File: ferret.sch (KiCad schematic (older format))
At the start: 75 parts, among them J1 USB_C_Receptacle, J2 Jack-DC, J3 GND/RS485 L, J4 BAT+ L, J5 GND/RS485 R, J6 BAT+ R, J7 BAT, J8 Jack-DC, J9 SYS, Q1 40V, Q2 40V, Q3 40V, Q4 40V, Q5 40V, U1 FUSB307BMPX, U2 TPD6S300A, U3 BQ25792, U4 TPS560430X3F

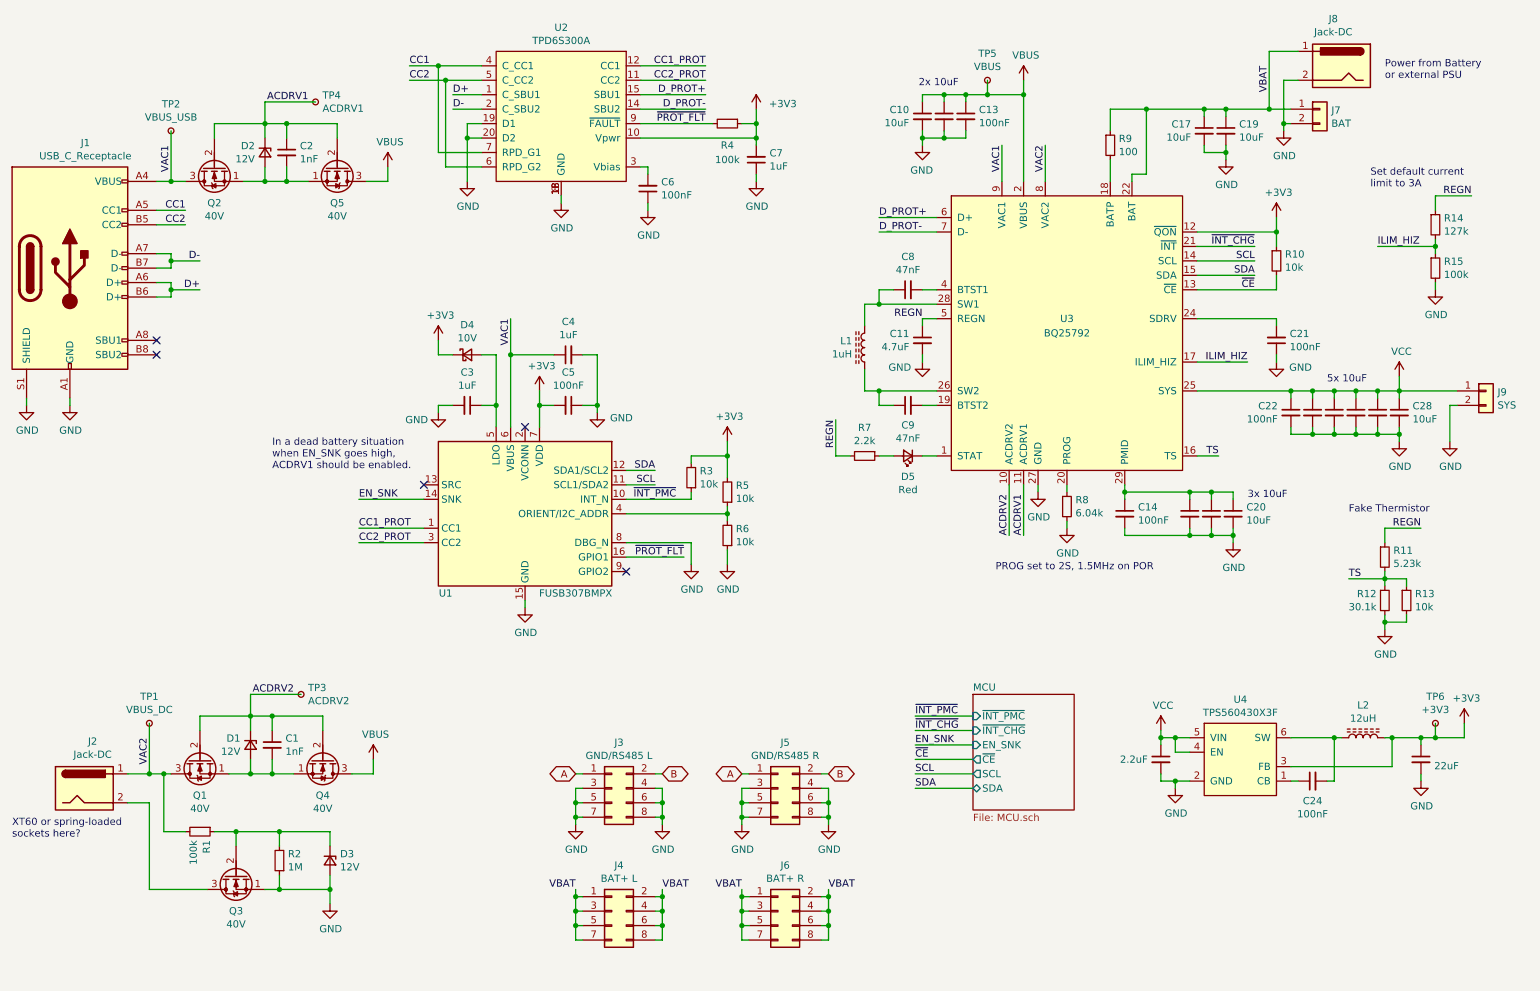
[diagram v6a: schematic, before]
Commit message: Split up ferret sheets and add some features
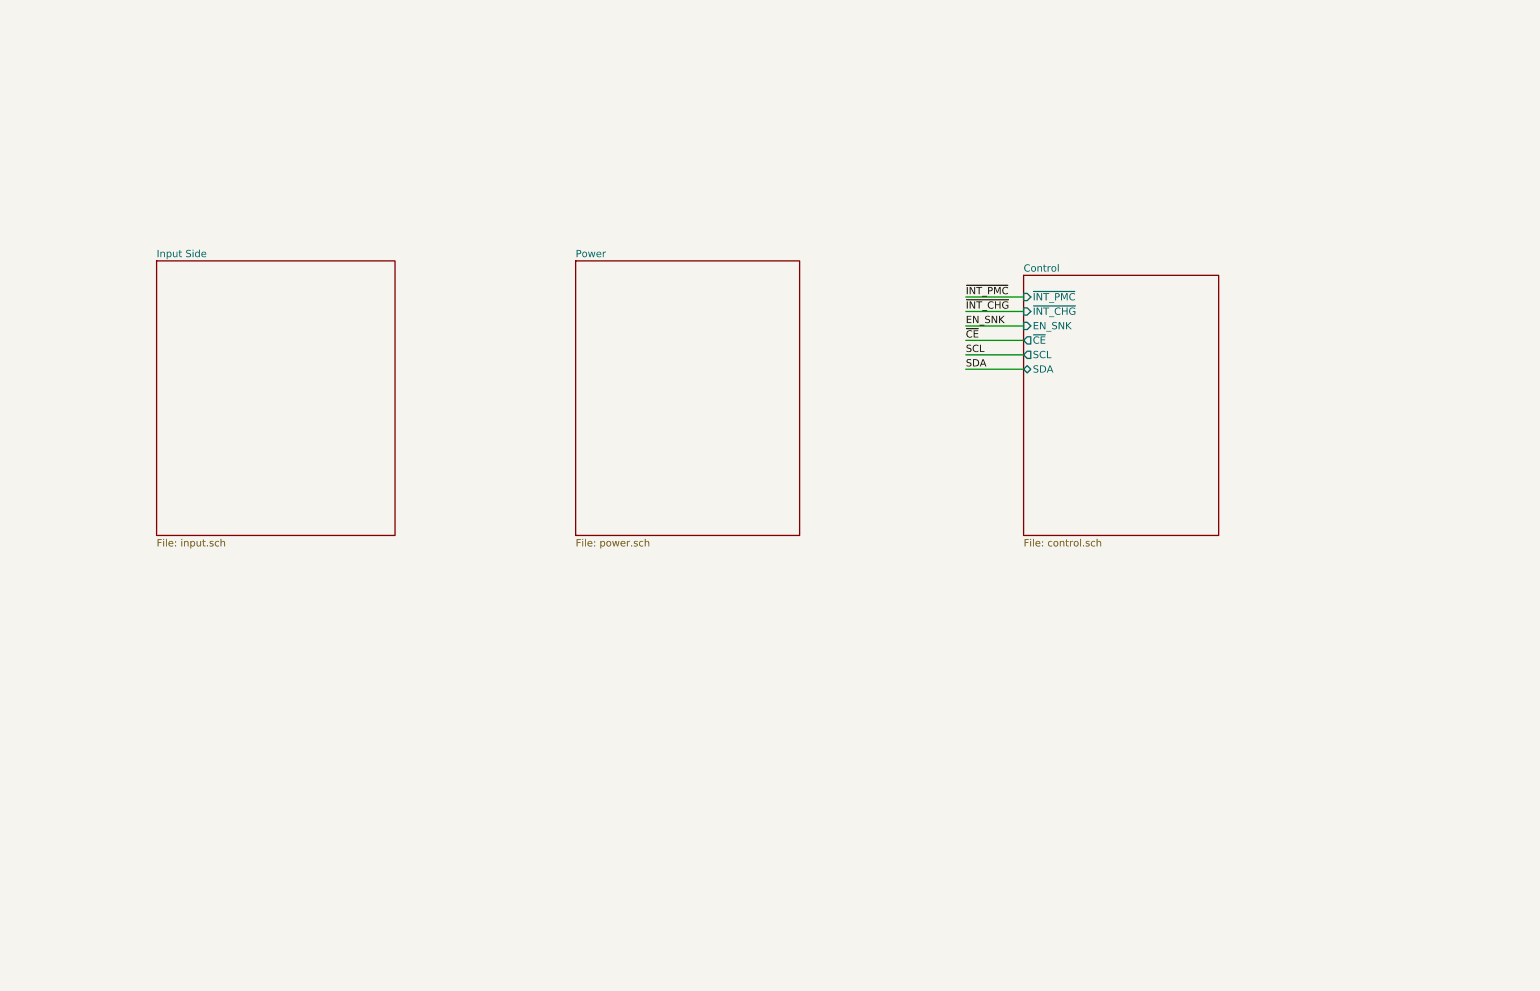
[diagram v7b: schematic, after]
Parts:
- removed C1, C2: 1nF, Capacitor_SMD:C_0603_1608Metric, symbol Device:C_Small
- removed C10, C12, C16, C17, C18, C19, C20, C23, C25, C26, C27, C28: 10uF, Capacitor_SMD:C_0805_2012Metric, symbol Device:C_Small
- removed C11: 4.7uF, Capacitor_SMD:C_0603_1608Metric, symbol Device:C_Small
- removed C13, C14, C21, C22, C24, C5, C6: 100nF, Capacitor_SMD:C_0603_1608Metric, symbol Device:C_Small
- removed C15: 2.2uF, Capacitor_SMD:C_0805_2012Metric, symbol Device:C_Small
- removed C29: 22uF, Capacitor_SMD:C_0805_2012Metric, symbol Device:C_Small
- removed C3, C4, C7: 1uF, Capacitor_SMD:C_0603_1608Metric, symbol Device:C_Small
- removed C8, C9: 47nF, Capacitor_SMD:C_0603_1608Metric, symbol Device:C_Small
- removed D1, D2, D3: 12V, Diode_SMD:D_SOD-523, symbol Device:D_Zener_Small
- removed D4: 10V, Diode_SMD:D_SOD-123, symbol Device:D_Schottky_Small
- removed D5: Red, LED_SMD:LED_0603_1608Metric_Castellated, symbol Device:LED_Small
- removed J1: USB_C_Receptacle, Connector_USB:USB_C_Receptacle_XKB_U262-16XN-4BVC11, symbol Connector:USB_C_Receptacle_USB2.0
- removed J2, J8: Jack-DC, Connector_BarrelJack:BarrelJack_Horizontal, symbol Connector:Jack-DC
- removed J3: GND/RS485 L, Connector_PinHeader_2.54mm:PinHeader_2x04_P2.54mm_Horizontal, symbol Connector_Generic:Conn_02x04_Odd_Even
- removed J4: BAT+ L, Connector_PinHeader_2.54mm:PinHeader_2x04_P2.54mm_Horizontal, symbol Connector_Generic:Conn_02x04_Odd_Even
- removed J5: GND/RS485 R, Connector_PinHeader_2.54mm:PinHeader_2x04_P2.54mm_Horizontal, symbol Connector_Generic:Conn_02x04_Odd_Even
- removed J6: BAT+ R, Connector_PinHeader_2.54mm:PinHeader_2x04_P2.54mm_Horizontal, symbol Connector_Generic:Conn_02x04_Odd_Even
- removed J7: BAT, Automated:Conn_AMASS_XT60PW-F20, symbol Connector_Generic:Conn_01x02
- removed J9: SYS, Connector_PinSocket_2.54mm:PinSocket_1x02_P2.54mm_Vertical, symbol Connector_Generic:Conn_01x02
- removed L1: 1uH, Inductor_SMD:L_Bourns_SRP1245A, symbol Device:L_Core_Ferrite
- removed L2: 12uH, Inductor_SMD:L_Bourns_SRN6045TA, symbol Device:L_Core_Ferrite
- removed Q1, Q2, Q3, Q4, Q5: 40V, Package_SO:Vishay_PowerPAK_1212-8_Single, symbol Device:Q_NMOS_SGD
- removed R1, R15, R4: 100k, Resistor_SMD:R_0603_1608Metric, symbol Device:R_Small
- removed R10, R13, R3, R5, R6: 10k, Resistor_SMD:R_0603_1608Metric, symbol Device:R_Small
- removed R11: 5.23k, Resistor_SMD:R_0603_1608Metric, symbol Device:R_Small
- removed R12: 30.1k, Resistor_SMD:R_0603_1608Metric, symbol Device:R_Small
- removed R14: 127k, Resistor_SMD:R_0603_1608Metric, symbol Device:R_Small
- removed R2: 1M, Resistor_SMD:R_0603_1608Metric, symbol Device:R_Small
- removed R7: 2.2k, Resistor_SMD:R_0603_1608Metric, symbol Device:R_Small
- removed R8: 6.04k, Resistor_SMD:R_0603_1608Metric, symbol Device:R_Small
- removed R9: 100, Resistor_SMD:R_0603_1608Metric, symbol Device:R_Small
- removed TP1: VBUS_DC, TestPoint:TestPoint_THTPad_D2.0mm_Drill1.0mm, symbol Connector:TestPoint_Small
- removed TP2: VBUS_USB, TestPoint:TestPoint_THTPad_D2.0mm_Drill1.0mm, symbol Connector:TestPoint_Small
- removed TP3: ACDRV2, TestPoint:TestPoint_THTPad_D2.0mm_Drill1.0mm, symbol Connector:TestPoint_Small
- removed TP4: ACDRV1, TestPoint:TestPoint_THTPad_D2.0mm_Drill1.0mm, symbol Connector:TestPoint_Small
- removed TP5: VBUS, TestPoint:TestPoint_THTPad_D2.0mm_Drill1.0mm, symbol Connector:TestPoint_Small
- removed TP6: +3V3, TestPoint:TestPoint_THTPad_D2.0mm_Drill1.0mm, symbol Connector:TestPoint_Small
- removed U1: FUSB307BMPX, Package_DFN_QFN:WQFN-16-1EP_3x3mm_P0.5mm_EP1.75x1.75mm, symbol Interface_USB:FUSB307BMPX
- removed U2: TPD6S300A, Package_DFN_QFN:QFN-20-1EP_3x3mm_P0.4mm_EP1.65x1.65mm, symbol meansOfCircuitDesign:TPD6S300A
- removed U3: BQ25792, Automated:Texas_VQFN-HR_RQM_4x4mm_P0.40-0.45mm, symbol meansOfCircuitDesign:BQ25792
- removed U4: TPS560430X3F, Package_TO_SOT_SMD:SOT-23-6, symbol meansOfCircuitDesign:TPS560430X3F
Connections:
- no-connect marks 5 -> 0
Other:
- note removed: "2x 10uF"
- note removed: "3x 10uF"
- note removed: "5x 10uF"
- note removed: "Fake Thermistor"
- note removed: "In a dead battery situation\nwhen EN_SNK goes high,\nACDRV1 should be enabled."
- note removed: "PROG set to 2S, 1.5MHz on POR"
- note removed: "Power from Battery\nor external PSU"
- note removed: "Set default current\nlimit to 3A"
- note removed: "XT60 or spring-loaded\nsockets here?"

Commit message: I'm pretty happy with it now, will place tomorrow
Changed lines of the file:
@@
 Comment4 ""
 $EndDescr
-Text Label 7300 3050 0    50   ~ 0
-~CE
-Text Label 7300 3250 0    50   ~ 0
-SDA
-Text Label 7300 3150 0    50   ~ 0
-SCL
-Text Label 7300 2850 0    50   ~ 0
-~INT_CHG
-Text Label 7300 2750 0    50   ~ 0
-~INT_PMC
-Text Label 7300 2950 0    50   ~ 0
-EN_SNK
-Wire Wire Line
-	7300 2750 7700 2750
-Wire Wire Line
-	7700 2850 7300 2850
-Wire Wire Line
-	7300 2950 7700 2950
-Wire Wire Line
-	7700 3050 7300 3050
-Wire Wire Line
-	7700 3150 7300 3150
-Wire Wire Line
-	7300 3250 7700 3250
 $Sheet
 S 1700 2500 1650 1900
@@
 F0 "Input Side" 50
 F1 "input.sch" 50
+F2 "D_PD+" B R 3350 3150 50
+F3 "D_PD-" B R 3350 3250 50
+F4 "USB_SEL" I R 3350 3900 50
+F5 "D_CHG+" B R 3350 2850 50
+F6 "D_CHG-" B R 3350 2950 50
+F7 "SBU2" B R 3350 4250 50
+F8 "SBU1" B R 3350 4150 50
+F9 "~INT_PMC" O R 3350 3750 50
+F10 "EN_SINK" I R 3350 4000 50
 $EndSheet
 $Sheet
-S 4600 2500 1550 1900
+S 4650 2500 1550 1900
 U 5F165A7A
 F0 "Power" 50
 F1 "power.sch" 50
+F2 "D+" B L 4650 3150 50
+F3 "D-" B L 4650 3250 50
+F4 "~INT_CHG" O R 6200 3650 50
+F5 "SCL" I R 6200 3150 50
+F6 "SDA" B R 6200 3250 50
+F7 "~CE" I R 6200 3450 50
 $EndSheet
 $Sheet
-S 7700 2600 1350 1800
+S 7550 2500 1600 1900
 U 5EF44CB5
 F0 "Control" 50
 F1 "control.sch" 50
-F2 "~INT_PMC" I L 7700 2750 50
-F3 "EN_SNK" I L 7700 2950 50
-F4 "~CE" O L 7700 3050 50
-F5 "SCL" O L 7700 3150 50
-F6 "SDA" B L 7700 3250 50
-F7 "~INT_CHG" I L 7700 2850 50
+F2 "~INT_PMC" I L 7550 3750 50
+F3 "EN_SNK" I L 7550 4000 50
+F4 "~CE" O L 7550 3450 50
+F5 "SCL" O L 7550 3150 50
+F6 "SDA" B L 7550 3250 50
+F7 "~INT_CHG" I L 7550 3650 50
+F8 "D-" B L 7550 2950 50
+F9 "D+" B L 7550 2850 50
+F10 "SBU1" B L 7550 4150 50
+F11 "SBU2" B L 7550 4250 50
+F12 "USB_SEL" O L 7550 3900 50
 $EndSheet
+Wire Wire Line
+	6200 3250 7550 3250
+Wire Wire Line
+	7550 3150 6200 3150
+Wire Wire Line
+	7550 3450 6200 3450
+Wire Wire Line
+	3350 3150 4650 3150
+Wire Wire Line
+	4650 3250 3350 3250
+Wire Wire Line
+	6200 3650 7550 3650
+Wire Wire Line
+	3350 2850 3900 2850
+Wire Wire Line
+	3900 2850 3900 2100
+Wire Wire Line
+	3900 2100 7000 2100
+Wire Wire Line
+	7000 2100 7000 2850
+Wire Wire Line
+	7000 2850 7550 2850
+Wire Wire Line
+	3350 2950 4000 2950
+Wire Wire Line
+	4000 2950 4000 2200
+Wire Wire Line
+	4000 2200 6900 2200
+Wire Wire Line
+	6900 2200 6900 2950
+Wire Wire Line
+	6900 2950 7550 2950
+Wire Wire Line
+	3350 4250 3900 4250
+Wire Wire Line
+	3900 4250 3900 5050
+Wire Wire Line
+	3900 5050 7000 5050
+Wire Wire Line
+	7000 5050 7000 4250
+Wire Wire Line
+	7000 4250 7550 4250
+Wire Wire Line
+	7550 4150 6900 4150
+Wire Wire Line
+	6900 4150 6900 4950
+Wire Wire Line
+	6900 4950 4000 4950
+Wire Wire Line
+	4000 4950 4000 4150
+Wire Wire Line
+	4000 4150 3350 4150
+Wire Wire Line
+	3350 4000 4100 4000
+Wire Wire Line
+	4100 4000 4100 4850
+Wire Wire Line
+	4100 4850 6800 4850
+Wire Wire Line
+	6800 4850 6800 4000
+Wire Wire Line
+	6800 4000 7550 4000
+Wire Wire Line
+	3350 3900 4200 3900
+Wire Wire Line
+	4200 3900 4200 4750
+Wire Wire Line
+	4200 4750 6700 4750
+Wire Wire Line
+	6700 4750 6700 3900
+Wire Wire Line
+	6700 3900 7550 3900
+Wire Wire Line
+	7550 3750 6600 3750
+Wire Wire Line
+	6600 3750 6600 4650
+Wire Wire Line
+	6600 4650 4300 4650
+Wire Wire Line
+	4300 4650 4300 3750
+Wire Wire Line
+	4300 3750 3350 3750
 $EndSCHEMATC
